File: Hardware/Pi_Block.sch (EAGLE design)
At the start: 50 parts, among them Q1 BSS138, U1 PCA9306, U2 EDISON_CONNECTOR_FULLMOUNTING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, U3 EDISON_CONNECTOR_FULLHEADER, U4 TPS62065, U5 MIC5219 3.3V

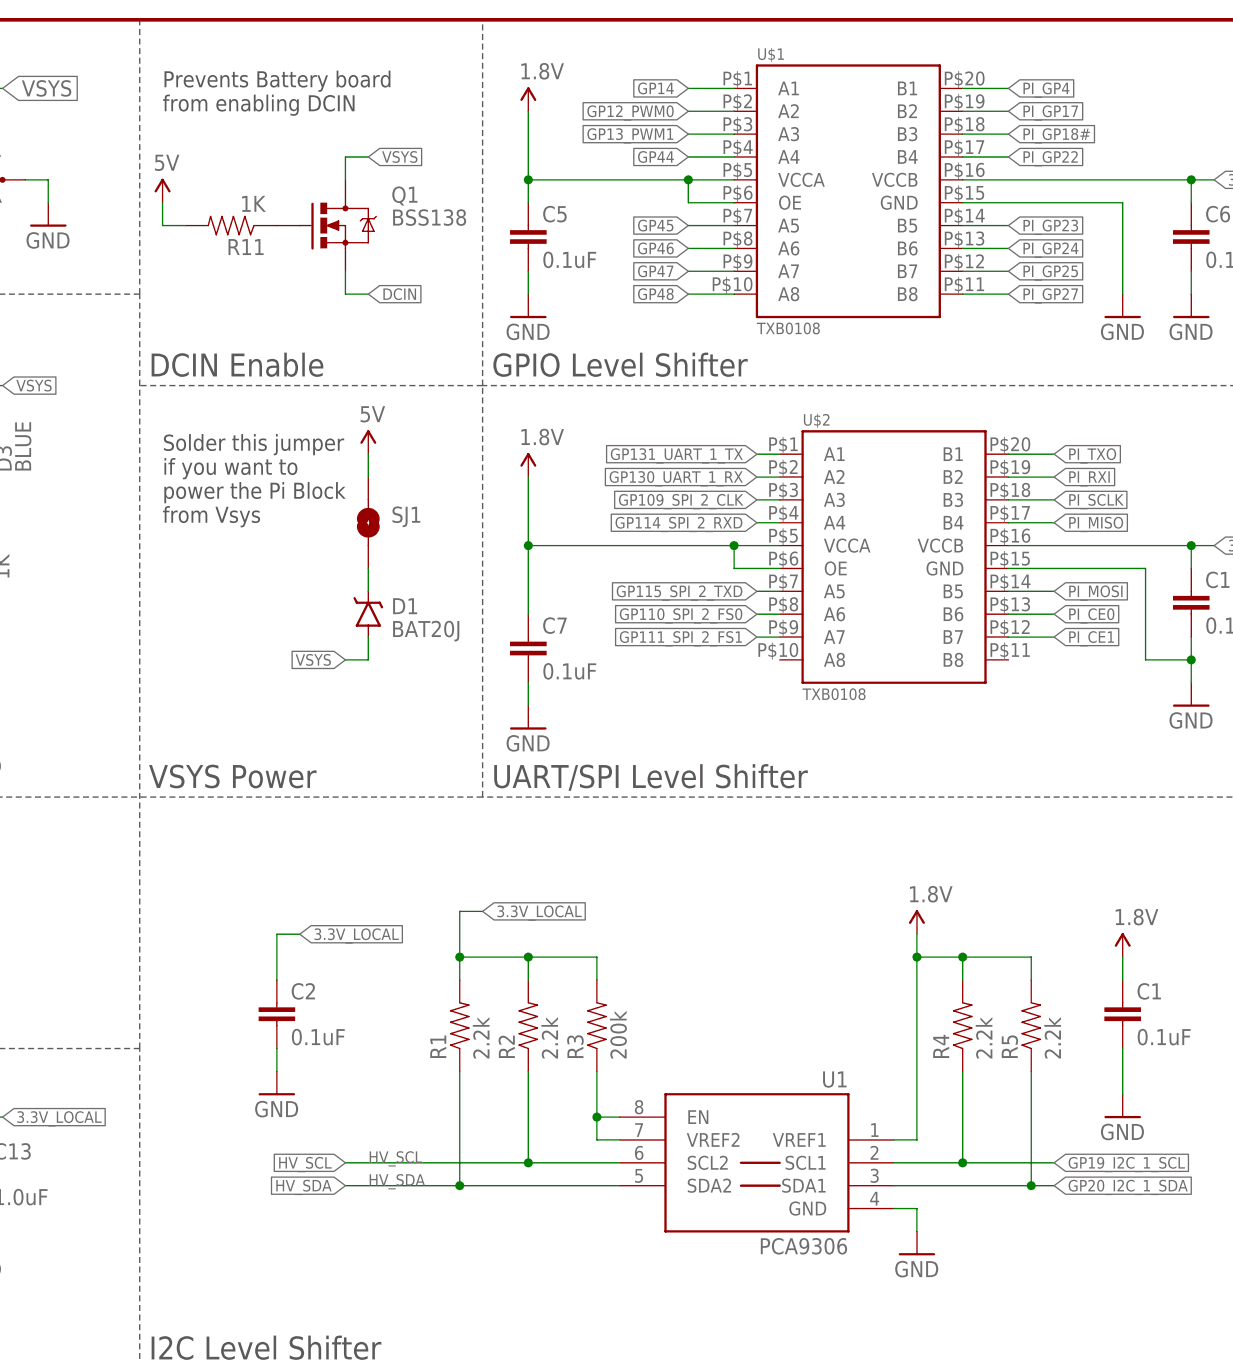
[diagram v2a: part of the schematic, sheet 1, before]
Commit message: Made R4 and R5 DNP. Added I2C PU solder jumper. Changed I2C PUs to 10k.
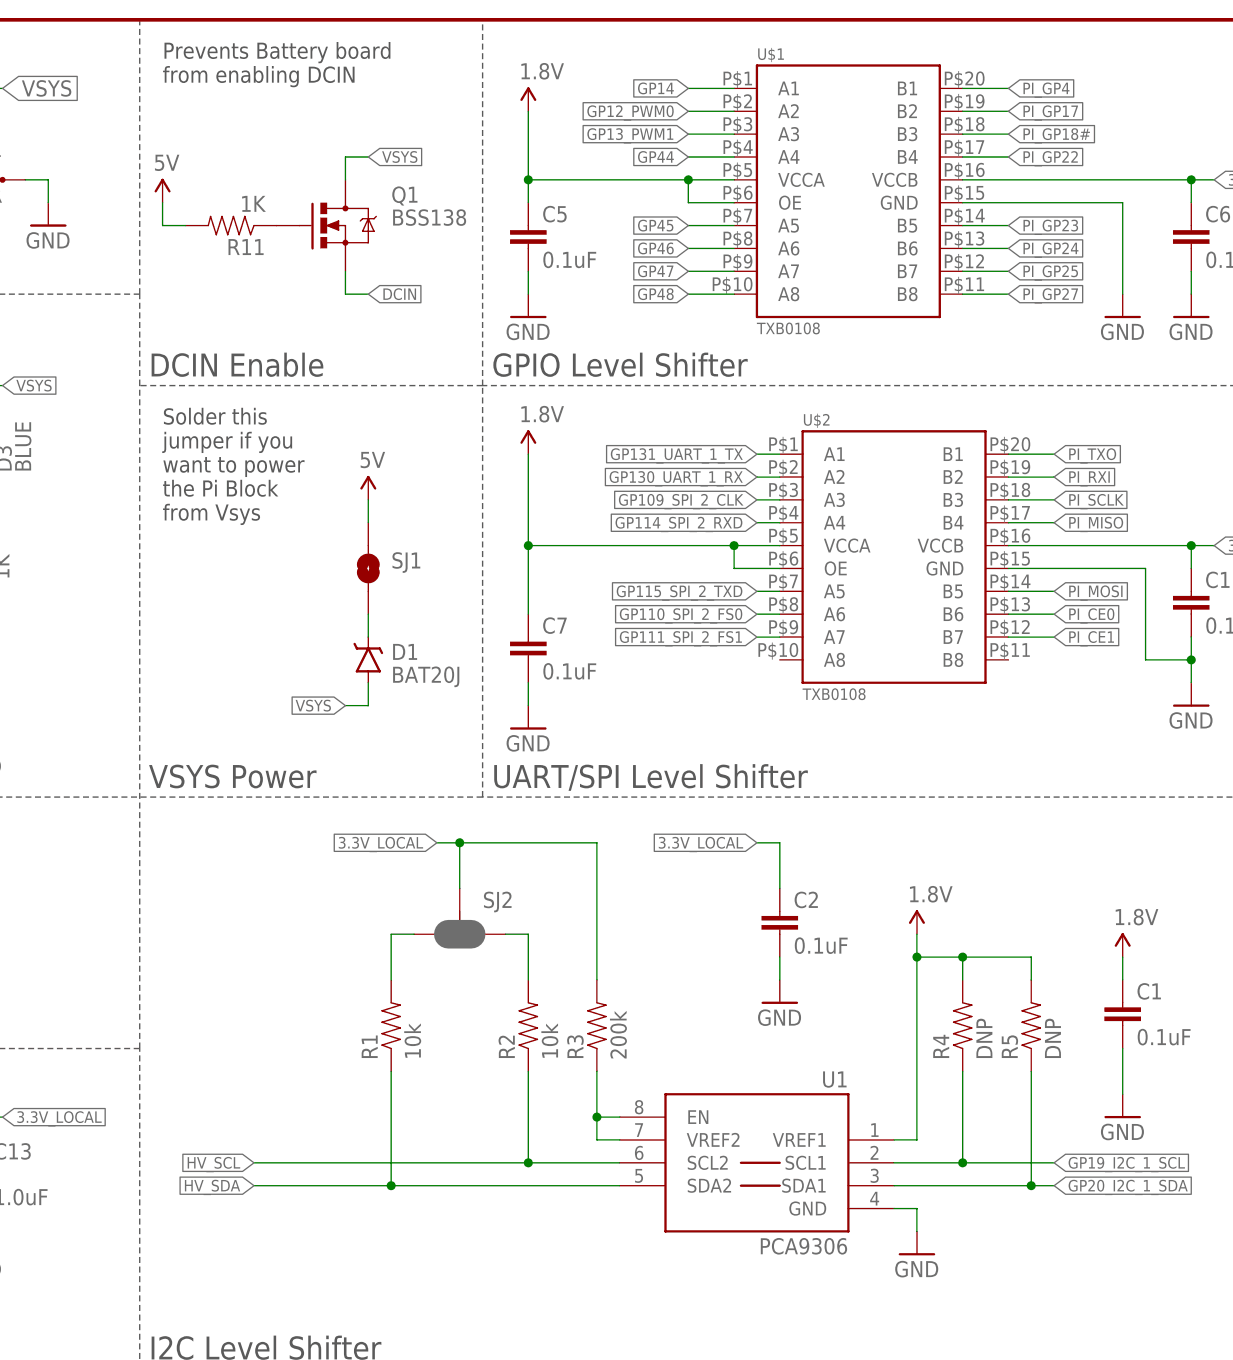
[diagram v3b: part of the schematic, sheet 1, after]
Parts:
- added SJ2: JUMPER-PAD-3-NC_BY_PASTE, SparkFun-Passives:JUMPER-PAD-3-NC_BY_PASTE
- LOGO3: value SFE_LOGO_FLAME.1_INCH -> SFE_LOGO_FLAME.2_INCH; device SparkFun-Aesthetics:SFE_LOGO_FLAME.1_INCH -> SparkFun-Aesthetics:SFE_LOGO_FLAME.2_INCH
- R1, R2: value 2.2k -> 10k; device SparkFun-Resistors:2.2KOHM1/10W1%(0603) -> SparkFun-Resistors:10KOHM1/10W1%(0603)0603
- R4, R5: value 2.2k -> DNP; device SparkFun-Resistors:2.2KOHM1/10W1%(0603) -> SparkFun-Resistors:RESISTOR0603-RES
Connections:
- new net N$4: R1.2, SJ2.3
- new net N$5: R2.2, SJ2.1
- net 3.3V_LOCAL: now also SJ2.2; no longer R1.2, R2.2
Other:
- moved on the sheet: C2, D1, R1, SJ1

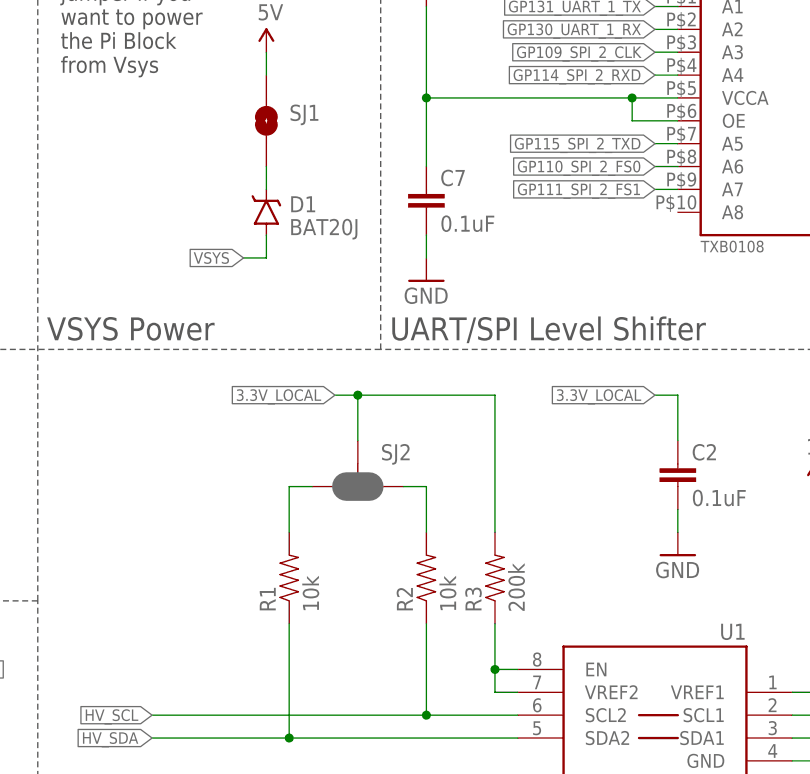
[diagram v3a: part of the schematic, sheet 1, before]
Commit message: Changed value from 10k to 10K to align with library
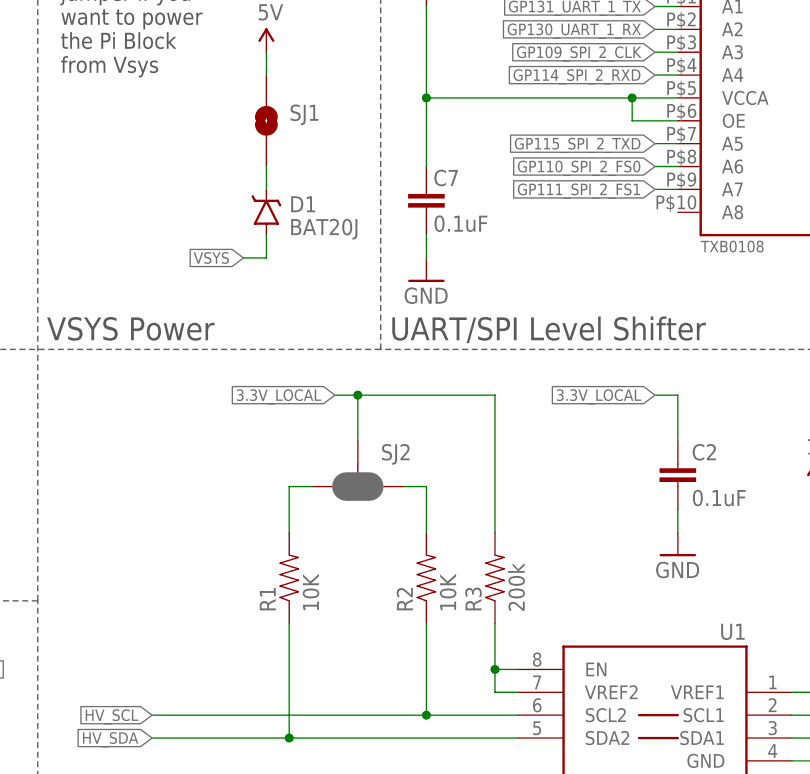
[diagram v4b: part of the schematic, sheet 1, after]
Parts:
- R1, R2: value 10k -> 10K
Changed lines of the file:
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@@
 <setting verticaltext="up"/>
 </settings>
-<grid distance="0.1" unitdist="inch" unit="inch" style="lines" multiple="1" display="no" altdistance="0.01" altunitdist="inch" altunit="inch"/>
+<grid distance="0.1" unitdist="inch" unit="inch" style="lines" multiple="1" display="yes" altdistance="0.01" altunitdist="inch" altunit="inch"/>
 <layers>
 <layer number="1" name="Top" color="4" fill="1" visible="no" active="no"/>
@@
 <part name="FID4" library="SparkFun-Aesthetics" deviceset="FIDUCIAL" device="1X2"/>
 <part name="JP1" library="SparkFun-Boards" deviceset="RASPBERRYPI-GPIO" device="PTH"/>
-<part name="R1" library="SparkFun-Resistors" deviceset="10KOHM1/10W1%(0603)" device="0603" value="10k"/>
-<part name="R2" library="SparkFun-Resistors" deviceset="10KOHM1/10W1%(0603)" device="0603" value="10k"/>
+<part name="R1" library="SparkFun-Resistors" deviceset="10KOHM1/10W1%(0603)" device="0603" value="10K"/>
+<part name="R2" library="SparkFun-Resistors" deviceset="10KOHM1/10W1%(0603)" device="0603" value="10K"/>
 <part name="U1" library="SparkFun-DigitalIC" deviceset="PCA9306" device="PCA9306DC-1:1" value="PCA9306"/>
 <part name="SUPPLY4" library="SparkFun-Aesthetics" deviceset="1.8V" device=""/>
@@
 <instance part="C6" gate="G$1" x="231.14" y="160.02"/>
 <instance part="C7" gate="G$1" x="157.48" y="114.3" smashed="yes">
-<attribute name="NAME" x="159.004" y="117.221" size="1.778" layer="95"/>
-<attribute name="VALUE" x="159.004" y="112.141" size="1.778" layer="96"/>
+<attribute name="NAME" x="158.242" y="117.221" size="1.778" layer="95"/>
+<attribute name="VALUE" x="158.242" y="112.141" size="1.778" layer="96"/>
 </instance>
 <instance part="C11" gate="G$1" x="231.14" y="119.38"/>

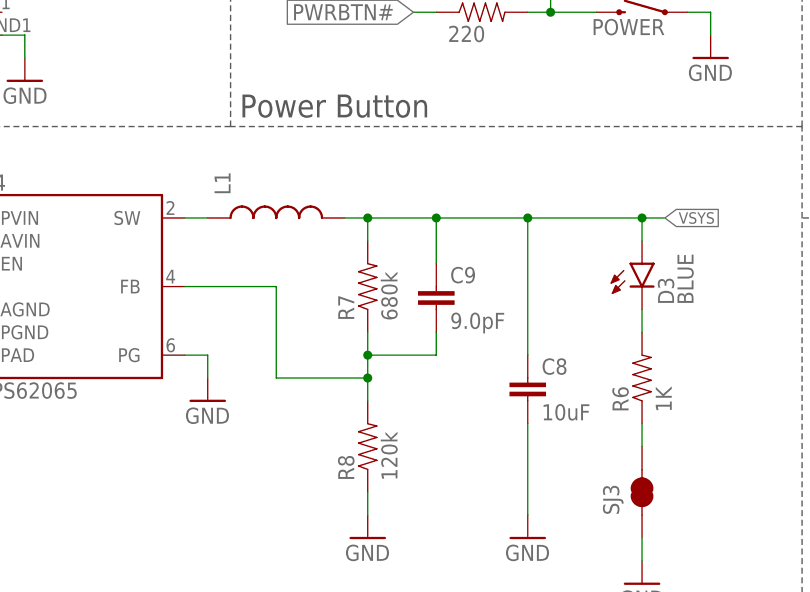
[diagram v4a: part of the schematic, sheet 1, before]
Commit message: Changed DC/DC output cap to 22uF. Added value to inductor.
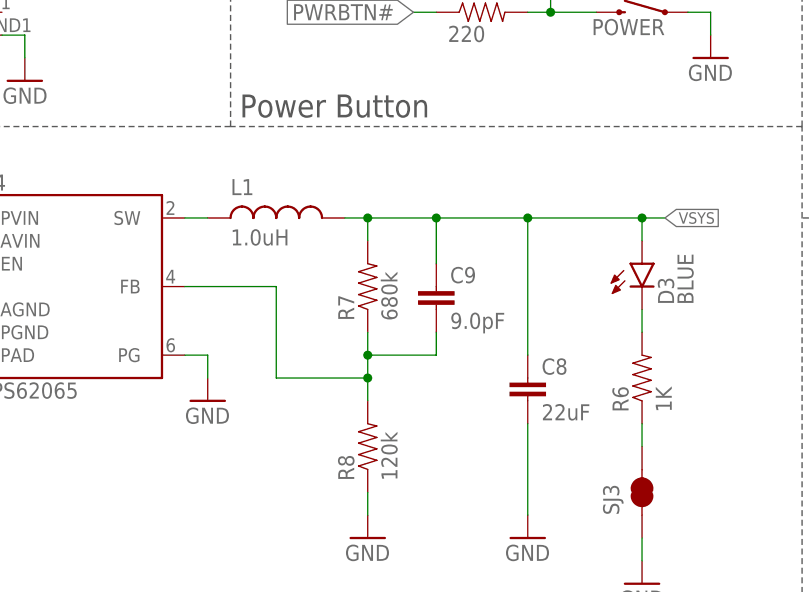
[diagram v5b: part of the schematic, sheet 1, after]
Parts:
- C8: value 10uF -> 22uF; device SparkFun-Capacitors:10UF-6.3V-20%(1206) -> SparkFun-Capacitors:22UF-6.3V-20%(0805)
- L1: value (none) -> 1.0uH; PROD_ID (none) -> NDUC-12274
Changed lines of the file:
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@@
 <part name="SJ3" library="SparkFun-Passives" deviceset="JUMPER-PAD-2-NC_BY_TRACE" device=""/>
 <part name="GND16" library="SparkFun-Aesthetics" deviceset="GND" device=""/>
-<part name="C8" library="SparkFun-Capacitors" deviceset="10UF-6.3V-20%(1206)" device="" value="10uF"/>
+<part name="C8" library="SparkFun-Capacitors" deviceset="22UF-6.3V-20%(0805)" device="" value="22uF"/>
 <part name="GND18" library="SparkFun-Aesthetics" deviceset="GND" device=""/>
 <part name="U4" library="Testing" deviceset="TPS62065" device=""/>
@@
 <part name="C10" library="SparkFun-Capacitors" deviceset="4.7UF-6.3V-10%(0603)" device="0603" value="4.7uF"/>
 <part name="GND19" library="SparkFun-Aesthetics" deviceset="GND" device=""/>
-<part name="L1" library="SparkFun-Passives" deviceset="INDUCTOR" device=""/>
+<part name="L1" library="SparkFun-Passives" deviceset="INDUCTOR" device="" value="1.0uH">
+<attribute name="PROD_ID" value="NDUC-12274"/>
+</part>
 <part name="U$1" library="Testing" deviceset="TXB0108" device=""/>
 <part name="U$2" library="Testing" deviceset="TXB0108" device=""/>
@@
 <instance part="C10" gate="G$1" x="7.62" y="134.62"/>
 <instance part="GND19" gate="1" x="66.04" y="109.22"/>
-<instance part="L1" gate="G$1" x="55.88" y="144.78" rot="R90"/>
+<instance part="L1" gate="G$1" x="55.88" y="144.78" smashed="yes" rot="R90">
+<attribute name="PROD_ID" x="55.88" y="144.78" size="1.778" layer="96" rot="R90" display="off"/>
+<attribute name="NAME" x="50.8" y="147.32" size="1.778" layer="95"/>
+<attribute name="VALUE" x="50.8" y="141.732" size="1.778" layer="96"/>
+</instance>
 <instance part="U$1" gate="G$1" x="200.66" y="167.64"/>
 <instance part="U$2" gate="G$1" x="205.74" y="127"/>
